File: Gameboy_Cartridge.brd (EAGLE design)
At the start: 49.3 x 48 mm, 10 parts, among them IC1 AT49F040J

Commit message: Other changes to make it prettier
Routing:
- net 4: track 71.2 -> 68.3 mm, vias 2 -> 0
- net 3: track 25.5 -> 26.7 mm, vias 2 -> 0
- net 5: track 22.6 -> 23.4 mm, vias 0 -> 2
- net C: track 43.1 -> 42.4 mm

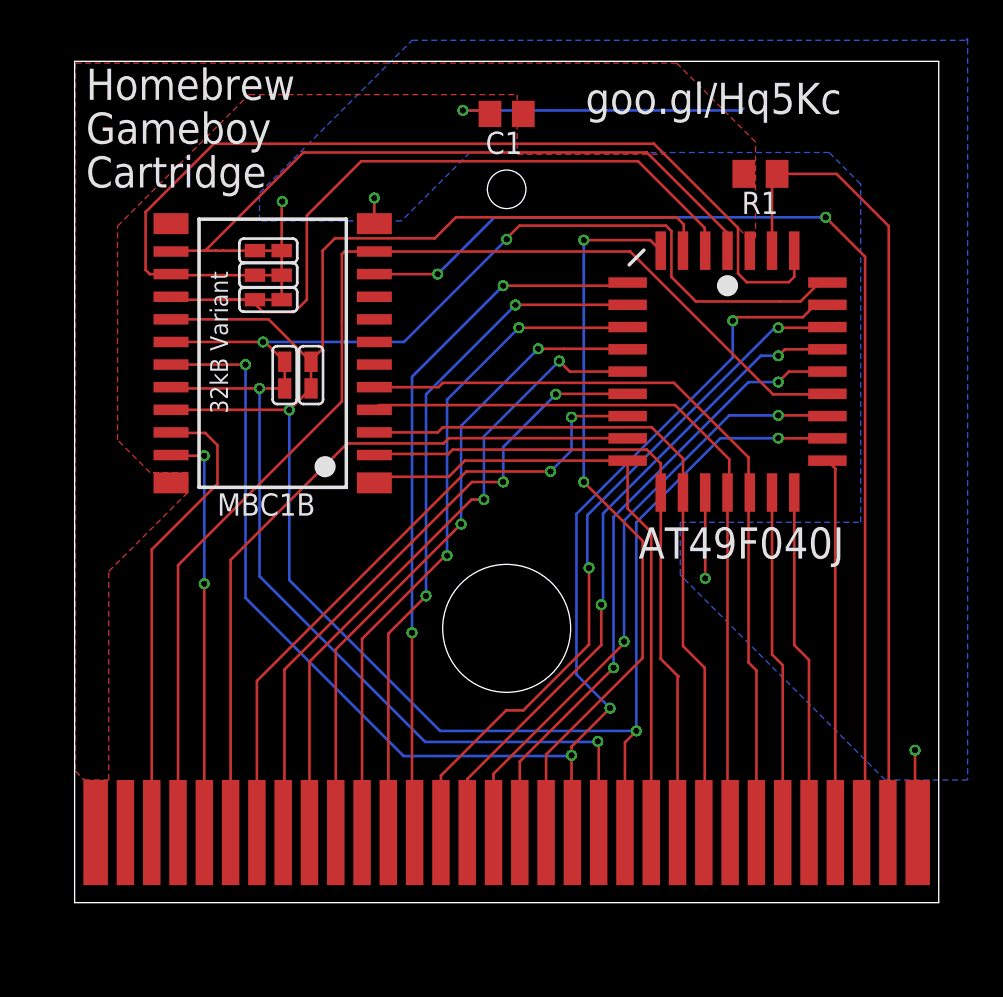
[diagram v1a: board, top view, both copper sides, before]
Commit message: Just make the entire bottom the GND plane and adjust VDD pour
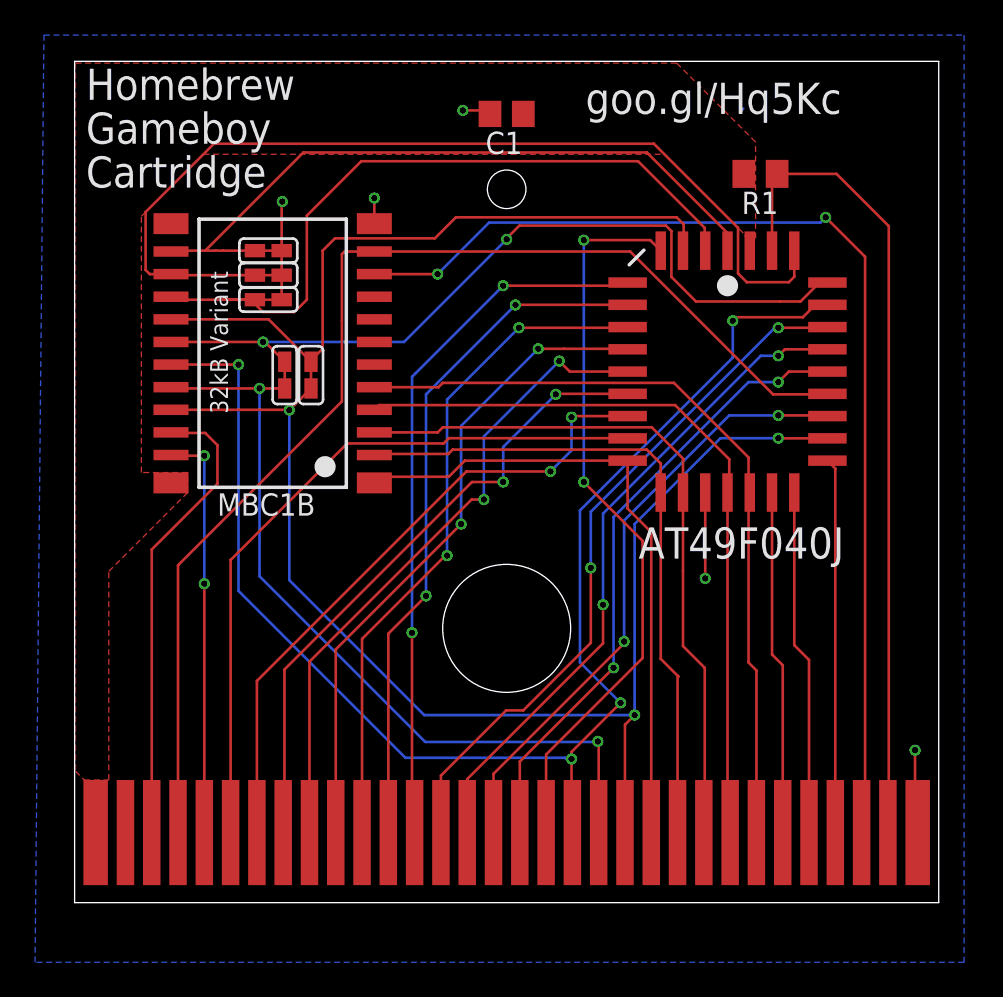
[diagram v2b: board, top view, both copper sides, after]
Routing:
- net GND: track 34.7 -> 18.8 mm
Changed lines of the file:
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@@
 <via x="23" y="45.2" extent="1-16" drill="0.35"/>
 <wire x1="39" y1="45.3" x2="38.9" y2="45.2" width="0.1524" layer="16"/>
-<wire x1="38.9" y1="45.2" x2="23" y2="45.2" width="0.1524" layer="16"/>
 <wire x1="23" y1="45.2" x2="24.35" y2="45.2" width="0.1524" layer="1"/>
 <wire x1="24.35" y1="45.2" x2="24.55" y2="45" width="0.1524" layer="1"/>
-<polygon width="0.1524" layer="16">
-<vertex x="51.8" y="7"/>
-<vertex x="47.1" y="7"/>
-<vertex x="35.4" y="18.7"/>
-<vertex x="35.4" y="21.7"/>
-<vertex x="45.7" y="21.7"/>
-<vertex x="45.7" y="41"/>
-<vertex x="43.9" y="42.8"/>
-<vertex x="23.4" y="42.8"/>
-<vertex x="19.5" y="38.9"/>
-<vertex x="11.4" y="38.9"/>
-<vertex x="11.4" y="40.5"/>
-<vertex x="20.1" y="49.2"/>
-<vertex x="51.7" y="49.2"/>
-<vertex x="51.8" y="49.3"/>
-</polygon>
 <wire x1="36.83" y1="23.4" x2="36.83" y2="18.5" width="0.1524" layer="1"/>
 <via x="36.83" y="18.5" extent="1-16" drill="0.35"/>
@@
 <via x="17.95" y="40.2" extent="1-16" drill="0.35"/>
 <wire x1="17.95" y1="40.2" x2="18.1" y2="40.2" width="0.1524" layer="16"/>
+<polygon width="0.1524" layer="16">
+<vertex x="-0.9" y="49.5"/>
+<vertex x="51.6" y="49.5"/>
+<vertex x="51.6" y="-3.4"/>
+<vertex x="-1.40670625" y="-3.4"/>
+</polygon>
 </signal>
 <signal name="VDD">
@@
 <vertex x="7.3" y="23.4"/>
 <vertex x="7.3" y="24.54"/>
-<vertex x="5.16" y="24.54"/>
-<vertex x="3.3" y="26.4"/>
-<vertex x="3.3" y="38.6"/>
-<vertex x="10.8" y="46.1"/>
-<vertex x="26.1" y="46.1"/>
-<vertex x="26.1" y="42.7"/>
+<vertex x="4.66" y="24.54"/>
+<vertex x="4.66" y="39.16"/>
+<vertex x="8.2" y="42.7"/>
 <vertex x="34.5" y="42.7"/>
 <vertex x="39.1" y="38.1"/>
@@
 <wire x1="14.338" y1="29.338" x2="13.12" y2="28.12" width="0.1524" layer="1"/>
 <wire x1="13.12" y1="28.12" x2="6.35" y2="28.12" width="0.1524" layer="1"/>
-<wire x1="32.25" y1="4" x2="32.25" y2="9.15" width="0.1524" layer="1"/>
-<wire x1="32.9" y1="9.8" x2="32.25" y2="9.15" width="0.1524" layer="1"/>
-<via x="32.9" y="9.8" extent="1-16" drill="0.35"/>
+<wire x1="32.25" y1="4" x2="32.25" y2="10.15" width="0.1524" layer="1"/>
+<wire x1="32.8" y1="10.7" x2="32.25" y2="10.15" width="0.1524" layer="1"/>
+<via x="32.8" y="10.7" extent="1-16" drill="0.35"/>
 <wire x1="41" y1="26.5" x2="37.7" y2="26.5" width="0.1524" layer="16"/>
-<wire x1="37.7" y1="26.5" x2="32.9" y2="21.7" width="0.1524" layer="16"/>
-<wire x1="32.9" y1="21.7" x2="32.9" y2="9.8" width="0.1524" layer="16"/>
+<wire x1="37.7" y1="26.5" x2="32.8" y2="21.6" width="0.1524" layer="16"/>
+<wire x1="32.8" y1="21.6" x2="32.8" y2="10.7" width="0.1524" layer="16"/>
 <via x="41" y="26.5" extent="1-16" drill="0.35"/>
 <wire x1="43.8" y1="26.49" x2="41.01" y2="26.49" width="0.1524" layer="1"/>
 <wire x1="41.01" y1="26.49" x2="41" y2="26.5" width="0.1524" layer="1"/>
-<wire x1="13.1" y1="18.4" x2="21.7" y2="9.8" width="0.1524" layer="16"/>
-<wire x1="21.7" y1="9.8" x2="32.9" y2="9.8" width="0.1524" layer="16"/>
+<wire x1="13.1" y1="18.4" x2="20.8" y2="10.7" width="0.1524" layer="16"/>
+<wire x1="20.8" y1="10.7" x2="32.8" y2="10.7" width="0.1524" layer="16"/>
 <wire x1="13.12" y1="28.12" x2="13.12" y2="28.1" width="0.1524" layer="1"/>
 <wire x1="13.12" y1="28.1" x2="13.1" y2="28.1" width="0.1524" layer="1"/>
@@
 <contactref element="IC1" pad="28"/>
 <wire x1="29.25" y1="4" x2="29.2" y2="4.05" width="0.1524" layer="1"/>
-<wire x1="29.2" y1="4.05" x2="29.2" y2="8.4" width="0.1524" layer="1"/>
-<via x="29.2" y="8.4" extent="1-16" drill="0.35"/>
-<via x="10.6" y="30.7" extent="1-16" drill="0.35"/>
-<wire x1="29.2" y1="8.4" x2="29.165" y2="8.365" width="0.1524" layer="16"/>
-<wire x1="29.165" y1="8.365" x2="19.6250875" y2="8.365" width="0.1524" layer="16"/>
-<wire x1="19.6250875" y1="8.365" x2="10.6" y2="17.3900875" width="0.1524" layer="16"/>
-<wire x1="10.6" y1="30.7" x2="10.6" y2="17.3900875" width="0.1524" layer="16"/>
-<wire x1="10.6" y1="30.7" x2="6.35" y2="30.7" width="0.1524" layer="1"/>
+<wire x1="29.2" y1="4.05" x2="29.2" y2="8.2" width="0.1524" layer="1"/>
+<via x="29.2" y="8.2" extent="1-16" drill="0.35"/>
+<via x="10.2" y="30.7" extent="1-16" drill="0.35"/>
+<wire x1="29.2" y1="8.2" x2="28.9" y2="8.2" width="0.1524" layer="16"/>
+<wire x1="28.9" y1="8.2" x2="28.835" y2="8.265" width="0.1524" layer="16"/>
+<wire x1="28.835" y1="8.265" x2="19.7250875" y2="8.265" width="0.1524" layer="16"/>
+<wire x1="19.7250875" y1="8.265" x2="10.2" y2="17.7900875" width="0.1524" layer="16"/>
+<wire x1="10.2" y1="30.7" x2="10.2" y2="17.7900875" width="0.1524" layer="16"/>
+<wire x1="10.2" y1="30.7" x2="6.35" y2="30.7" width="0.1524" layer="1"/>
 <wire x1="43.8" y1="34.11" x2="43.11" y2="34.11" width="0.1524" layer="1"/>
 <wire x1="38.6" y1="33.4" x2="38.4" y2="33.2" width="0.1524" layer="1"/>
@@
 <wire x1="42.4" y1="33.4" x2="38.6" y2="33.4" width="0.1524" layer="1"/>
 <wire x1="38.4" y1="33.2" x2="38.4" y2="31.1" width="0.1524" layer="16"/>
-<wire x1="38.4" y1="31.1" x2="29.4802" y2="22.1802" width="0.1524" layer="16"/>
-<wire x1="29.4802" y1="22.1802" x2="29.4802" y2="13.0198" width="0.1524" layer="16"/>
-<wire x1="29.4802" y1="13.0198" x2="31.4" y2="11.1" width="0.1524" layer="16"/>
-<via x="31.4" y="11.1" extent="1-16" drill="0.35"/>
-<wire x1="31.4" y1="11.1" x2="29.2" y2="8.9" width="0.1524" layer="1"/>
-<wire x1="29.2" y1="8.9" x2="29.2" y2="8.4" width="0.1524" layer="1"/>
+<wire x1="38.4" y1="31.1" x2="29.6802" y2="22.3802" width="0.1524" layer="16"/>
+<wire x1="29.6802" y1="22.3802" x2="29.6802" y2="13.7198" width="0.1524" layer="16"/>
+<wire x1="29.6802" y1="13.7198" x2="32" y2="11.4" width="0.1524" layer="16"/>
+<via x="32" y="11.4" extent="1-16" drill="0.35"/>
+<wire x1="32" y1="11.4" x2="29.2" y2="8.6" width="0.1524" layer="1"/>
+<wire x1="29.2" y1="8.6" x2="29.2" y2="8.2" width="0.1524" layer="1"/>
 </signal>
 <signal name="E">
@@
 <wire x1="45.95" y1="36.85" x2="43.7" y2="39.1" width="0.1524" layer="1"/>
 <via x="43.7" y="39.1" extent="1-16" drill="0.35"/>
-<wire x1="24.8" y1="39.1" x2="21.56" y2="35.86" width="0.1524" layer="16"/>
+<wire x1="24.5" y1="38.8" x2="21.56" y2="35.86" width="0.1524" layer="16"/>
 <via x="21.56" y="35.86" extent="1-16" drill="0.35"/>
-<wire x1="43.7" y1="39.1" x2="24.8" y2="39.1" width="0.1524" layer="16"/>
+<wire x1="43.7" y1="39.1" x2="43.4" y2="38.8" width="0.1524" layer="16"/>
+<wire x1="43.4" y1="38.8" x2="24.5" y2="38.8" width="0.1524" layer="16"/>
 </signal>
 <signal name="4">
@@
 <contactref element="IC1" pad="27"/>
 <wire x1="21.75" y1="4" x2="21.75" y2="7.25" width="0.1524" layer="1"/>
-<via x="30.2" y="19.1" extent="1-16" drill="0.35"/>
+<via x="30.3" y="19.1" extent="1-16" drill="0.35"/>
 <wire x1="25.4698" y1="10.9698" x2="26.44865625" y2="10.9698" width="0.1524" layer="1"/>
-<wire x1="26.44865625" y1="10.9698" x2="30.2" y2="14.72114375" width="0.1524" layer="1"/>
+<wire x1="26.44865625" y1="10.9698" x2="30.3" y2="14.82114375" width="0.1524" layer="1"/>
 <wire x1="21.75" y1="7.25" x2="25.4698" y2="10.9698" width="0.1524" layer="1"/>
-<wire x1="30.2" y1="14.72114375" x2="30.2" y2="19.1" width="0.1524" layer="1"/>
-<wire x1="30.1" y1="22.1" x2="30.1" y2="19.2" width="0.1524" layer="16"/>
-<wire x1="30.2" y1="19.1" x2="30.1" y2="19.2" width="0.1524" layer="16"/>
+<wire x1="30.3" y1="19.1" x2="30.3" y2="14.82114375" width="0.1524" layer="1"/>
+<wire x1="30.3" y1="22.3" x2="30.3" y2="19.3" width="0.1524" layer="16"/>
+<wire x1="30.3" y1="19.1" x2="30.3" y2="19.3" width="0.1524" layer="16"/>
 <wire x1="40.8" y1="32.8" x2="41" y2="32.8" width="0.1524" layer="16"/>
-<wire x1="40.8" y1="32.8" x2="30.1" y2="22.1" width="0.1524" layer="16"/>
+<wire x1="40.8" y1="32.8" x2="30.3" y2="22.3" width="0.1524" layer="16"/>
 <via x="41" y="32.8" extent="1-16" drill="0.35"/>
 <wire x1="41" y1="32.8" x2="43.76" y2="32.8" width="0.1524" layer="1"/>
@@
 <contactref element="IC1" pad="26"/>
 <wire x1="23.25" y1="4" x2="23.25" y2="7.05" width="0.1524" layer="1"/>
-<wire x1="23.25" y1="7.05" x2="30.9" y2="14.7" width="0.1524" layer="1"/>
-<wire x1="30.9" y1="14.7" x2="30.9" y2="17" width="0.1524" layer="1"/>
-<via x="30.9" y="17" extent="1-16" drill="0.35"/>
-<wire x1="30.9" y1="17" x2="31" y2="17.1" width="0.1524" layer="16"/>
+<wire x1="23.25" y1="7.05" x2="31" y2="14.8" width="0.1524" layer="1"/>
+<wire x1="31" y1="17" x2="31" y2="14.8" width="0.1524" layer="1"/>
+<via x="31" y="17" extent="1-16" drill="0.35"/>
+<wire x1="31" y1="17" x2="31" y2="17.1" width="0.1524" layer="16"/>
 <wire x1="31" y1="22.2" x2="31" y2="17.1" width="0.1524" layer="16"/>
 <wire x1="40" y1="31.2" x2="41" y2="31.2" width="0.1524" layer="16"/>
